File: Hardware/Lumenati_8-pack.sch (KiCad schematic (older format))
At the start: 26 parts, among them J1 CI, J2 DI, J3 5V, J4 GND, J5 CO, J6 DO, J7 5V, J8 GND, U1 APA102, U2 APA102, U3 APA102, U4 APA102, U5 APA102, U6 APA102, U7 APA102, U8 APA102

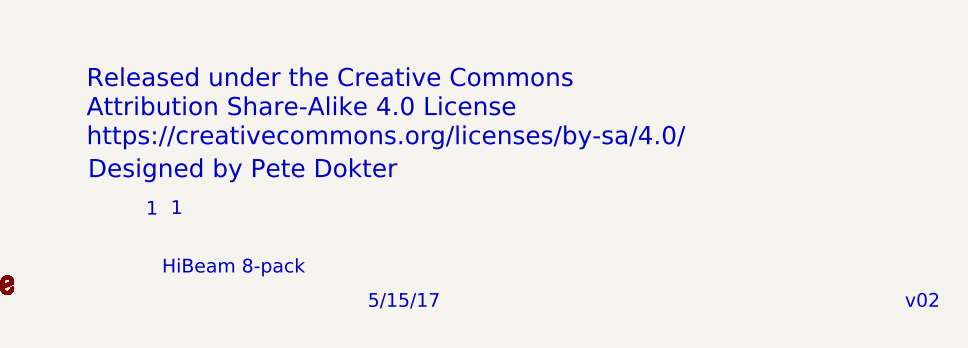
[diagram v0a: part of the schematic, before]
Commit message: Changed all the names to Lumenati, updated version to v10.
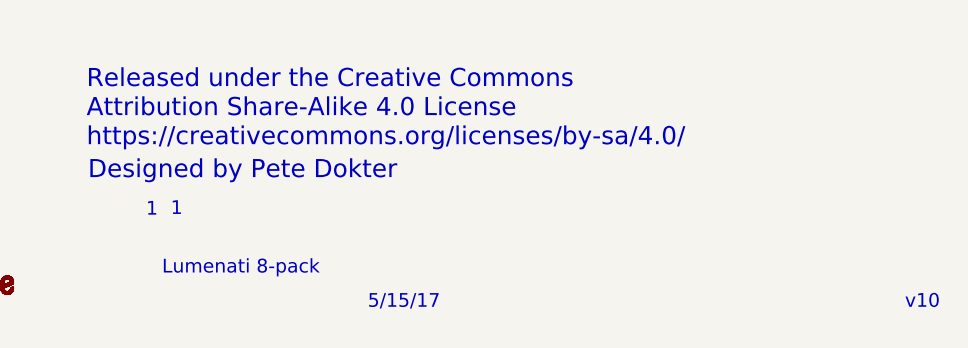
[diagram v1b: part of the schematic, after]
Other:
- note added: "Lumenati 8-pack"
- note added: "v10"
- note removed: "HiBeam 8-pack"
- note removed: "v02"
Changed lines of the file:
@@
 $EndComp
 Text Notes 10600 7650 0    60   ~ 0
-v02
+v10
 Text Notes 8250 7650 0    60   ~ 0
 5/15/17
 Text Notes 7350 7500 0    60   ~ 0
-HiBeam 8-pack
+Lumenati 8-pack
 $Comp
 L +5V #PWR?

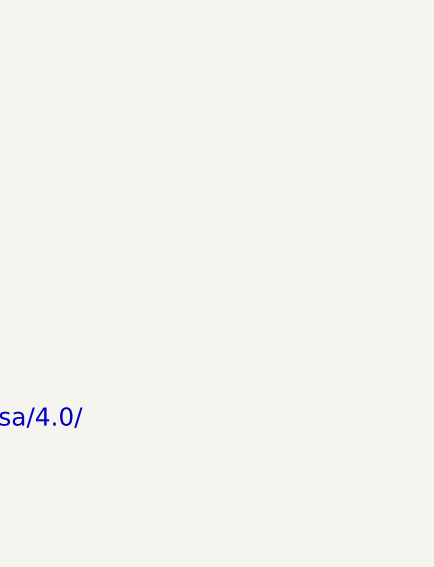
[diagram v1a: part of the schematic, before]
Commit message: Added Fiducials to schematic.
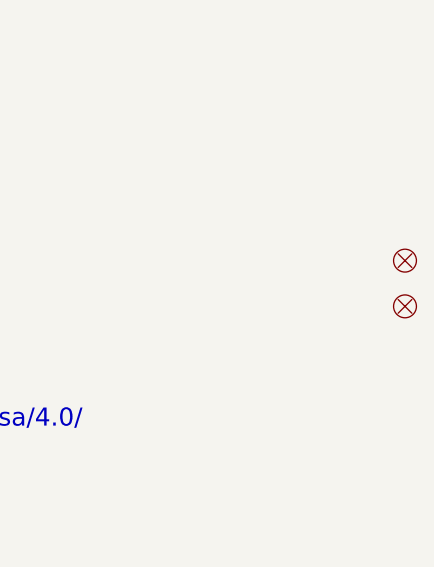
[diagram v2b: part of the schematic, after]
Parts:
- added FD? (x2): FIDUCIAL1X2, FIDUCIAL-1X2, symbol FIDUCIAL1X2
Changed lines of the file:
@@
 LIBS:contrib
 LIBS:valves
-LIBS:apa102-pov-cache
-LIBS:APA102
+LIBS:SparkFun-Aesthetics - Copy
 LIBS:SparkFun-Aesthetics
-LIBS:SparkFun-AnalogIC
+LIBS:SparkFun-Batteries
 LIBS:SparkFun-Boards
 LIBS:SparkFun-Capacitors
+LIBS:SparkFun-Clocks
+LIBS:SparkFun-Coils
 LIBS:SparkFun-Connectors
-LIBS:SparkFun-DigitalIC
 LIBS:SparkFun-DiscreteSemi
+LIBS:SparkFun-Displays
 LIBS:SparkFun-Electromechanical
-LIBS:SparkFun-FreqCtrl
+LIBS:SparkFun-Fuses
+LIBS:SparkFun-GPS
+LIBS:SparkFun-Hardware
+LIBS:SparkFun-IC-Amplifiers
+LIBS:SparkFun-IC-Comms
+LIBS:SparkFun-IC-Conversion
+LIBS:SparkFun-IC-Logic
+LIBS:SparkFun-IC-Memory
+LIBS:SparkFun-IC-Microcontroller
+LIBS:SparkFun-IC-Power
+LIBS:SparkFun-IC-Special-Function
+LIBS:SparkFun-Jumpers
 LIBS:SparkFun-LED
-LIBS:SparkFun-Passives
-LIBS:SparkFun-PowerIC
+LIBS:SparkFun-PowerSymbols
 LIBS:SparkFun-Resistors
 LIBS:SparkFun-RF
 LIBS:SparkFun-Sensors
-LIBS:HiBeam_8-pack_v02-cache
-EELAYER 26 0
+LIBS:SparkFun-Switches
+LIBS:Lumenati_8-pack-cache
+EELAYER 25 0
 EELAYER END
 $Descr A4 11693 8268
@@
 	1    0    0    -1
 $EndComp
+$Comp
+L FIDUCIAL1X2 FD?
+U 1 1 59970D49
+P 11050 6200
+F 0 "FD?" H 11050 6300 45  0001 C CNN
+F 1 "FIDUCIAL1X2" H 11050 6100 45  0001 C CNN
+F 2 "FIDUCIAL-1X2" H 11050 6350 20  0001 C CNN
+F 3 "" H 11050 6200 60  0001 C CNN
+F 4 "XXX-00000" H 11050 6400 60  0001 C CNN "Field4"
+	1    11050 6200
+	1    0    0    -1
+$EndComp
+$Comp
+L FIDUCIAL1X2 FD?
+U 1 1 59970EFF
+P 11050 6400
+F 0 "FD?" H 11050 6500 45  0001 C CNN
+F 1 "FIDUCIAL1X2" H 11050 6300 45  0001 C CNN
+F 2 "FIDUCIAL-1X2" H 11050 6550 20  0001 C CNN
+F 3 "" H 11050 6400 60  0001 C CNN
+F 4 "XXX-00000" H 11050 6600 60  0001 C CNN "Field4"
+	1    11050 6400
+	1    0    0    -1
+$EndComp
